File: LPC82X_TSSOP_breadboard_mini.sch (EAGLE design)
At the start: 16 parts, among them Q1 12MHz

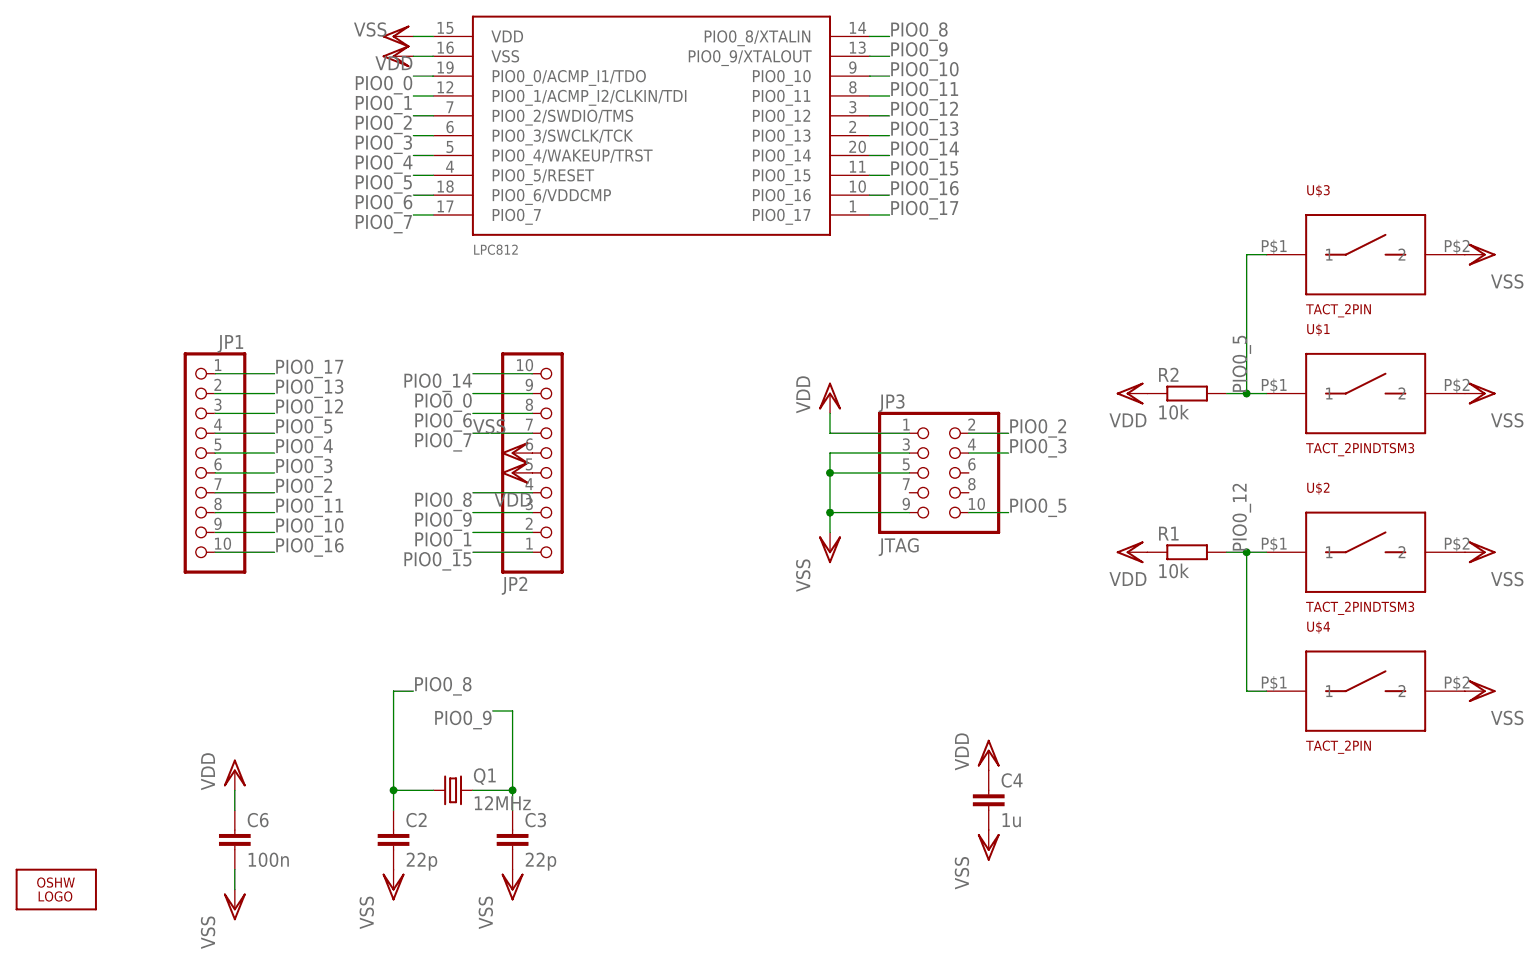
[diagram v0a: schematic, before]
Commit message: * started with lpc824 TSSOP breakout
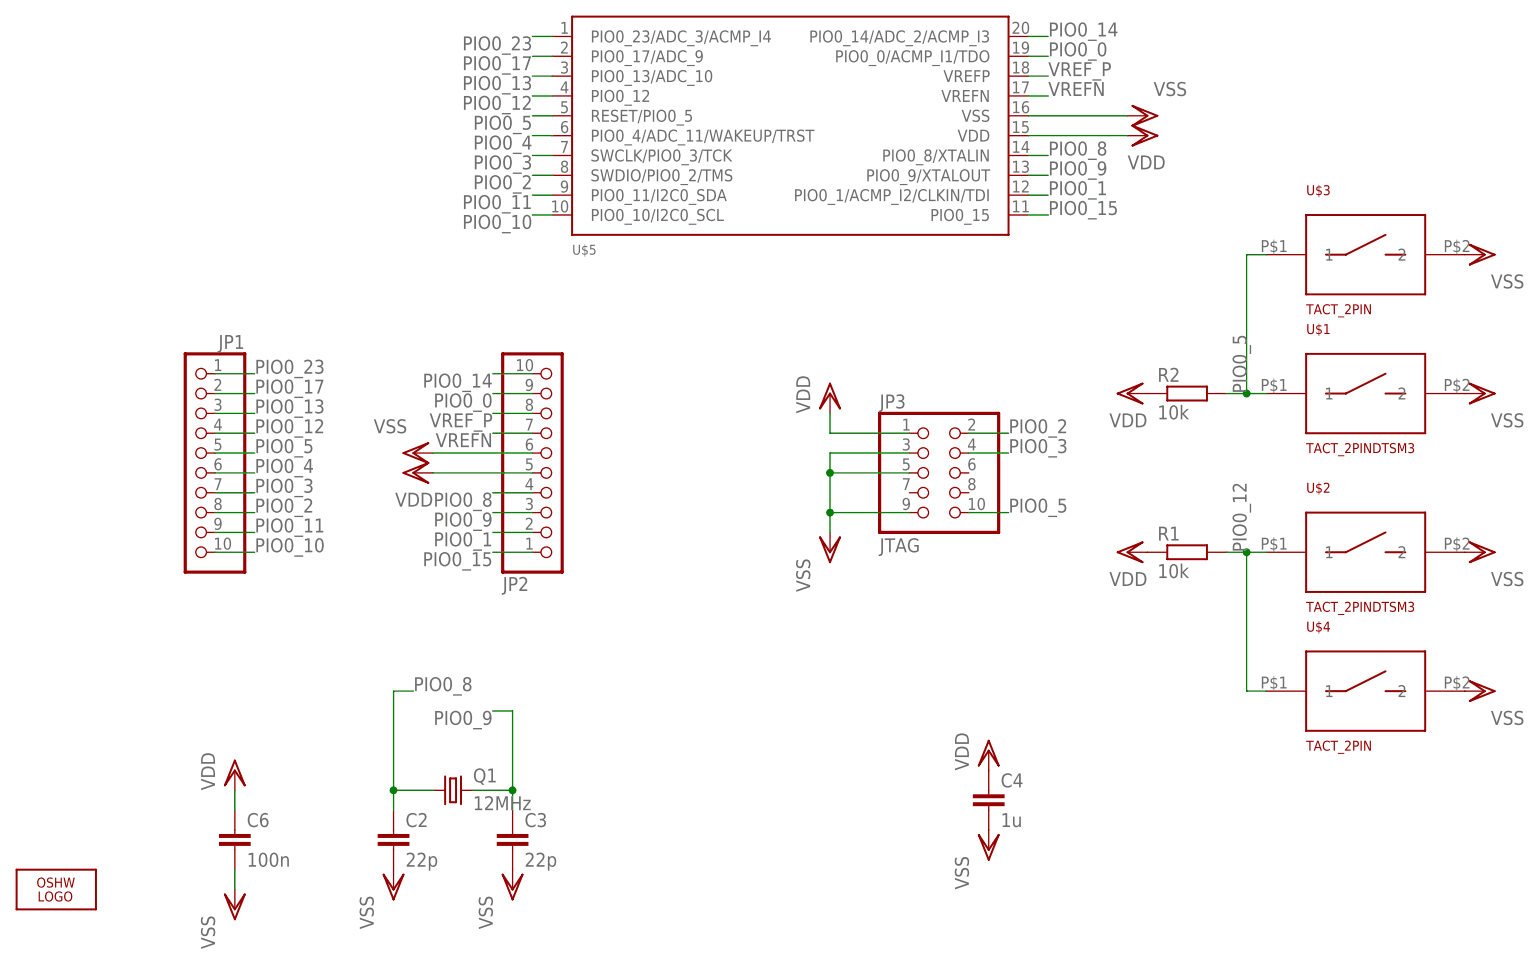
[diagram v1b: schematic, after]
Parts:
- removed LPC812: LPC812M101JDH20, LPC800:LPC812M101JDH20
- added U$5: LPC82XM101JDH20, LPC800:LPC82XM101JDH20
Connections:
- removed net PIO0_16: JP1.10, LPC812.PIO0_16
- removed net PIO0_6: JP2.8, LPC812.PIO0_6/VDDCMP
- removed net PIO0_7: JP2.7, LPC812.PIO0_7
- new net PIO0_23: JP1.1, U$5.PIO0_23/ADC_3/ACMP_I4
- new net VREFN: JP2.7, U$5.VREFN
- new net VREF_P: JP2.8, U$5.VREFP
- net PIO0_0: now also U$5.PIO0_0/ACMP_I1/TDO; no longer LPC812.PIO0_0/ACMP_I1/TDO
- net PIO0_1: now also U$5.PIO0_1/ACMP_I2/CLKIN/TDI; no longer LPC812.PIO0_1/ACMP_I2/CLKIN/TDI
- net PIO0_10: now also JP1.10, U$5.PIO0_10/I2C0_SCL; no longer JP1.9, LPC812.PIO0_10
- net PIO0_11: now also JP1.9, U$5.PIO0_11/I2C0_SDA; no longer JP1.8, LPC812.PIO0_11
- net PIO0_12: now also JP1.4, U$5.PIO0_12; no longer JP1.3, LPC812.PIO0_12
- net PIO0_13: now also JP1.3, U$5.PIO0_13/ADC_10; no longer JP1.2, LPC812.PIO0_13
- net PIO0_14: now also U$5.PIO0_14/ADC_2/ACMP_I3; no longer LPC812.PIO0_14
- net PIO0_15: now also U$5.PIO0_15; no longer LPC812.PIO0_15
- net PIO0_17: now also JP1.2, U$5.PIO0_17/ADC_9; no longer JP1.1, LPC812.PIO0_17
- net PIO0_2: now also JP1.8, U$5.SWDIO/PIO0_2/TMS; no longer JP1.7, LPC812.PIO0_2/SWDIO/TMS
- net PIO0_3: now also JP1.7, U$5.SWCLK/PIO0_3/TCK; no longer JP1.6, LPC812.PIO0_3/SWCLK/TCK
- net PIO0_4: now also JP1.6, U$5.PIO0_4/ADC_11/WAKEUP/TRST; no longer JP1.5, LPC812.PIO0_4/WAKEUP/TRST
- net PIO0_5: now also JP1.5, U$5.RESET/PIO0_5; no longer JP1.4, LPC812.PIO0_5/RESET
- net PIO0_8: now also U$5.PIO0_8/XTALIN; no longer LPC812.PIO0_8/XTALIN
- net PIO0_9: now also U$5.PIO0_9/XTALOUT; no longer LPC812.PIO0_9/XTALOUT
- net VDD: now also U$5.VDD; no longer LPC812.VDD
- net VSS: now also U$5.VSS; no longer LPC812.VSS
